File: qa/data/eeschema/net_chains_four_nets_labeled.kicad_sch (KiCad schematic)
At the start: 4 parts

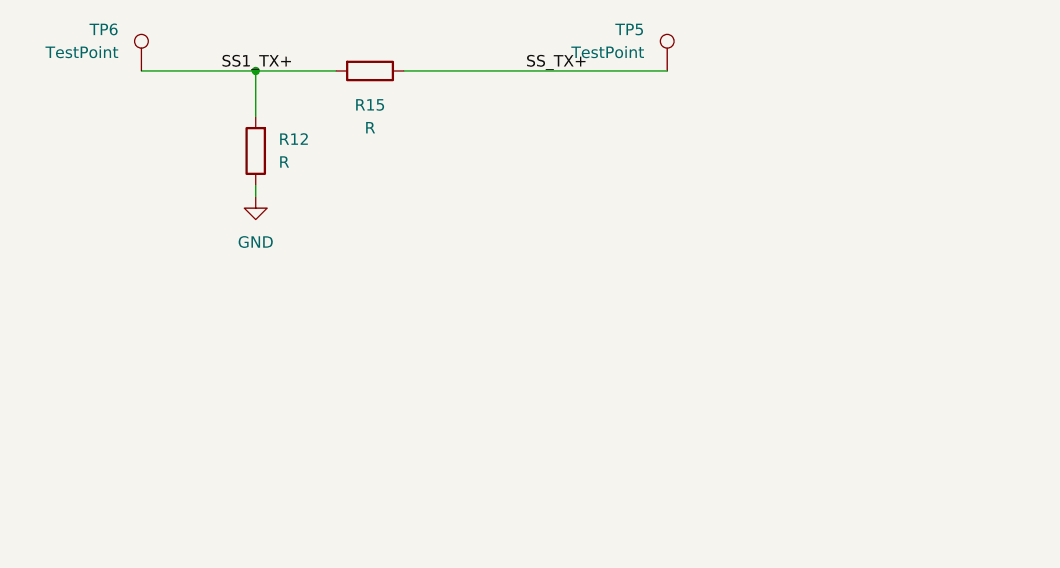
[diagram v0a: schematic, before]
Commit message: Fully rename signals to netchain
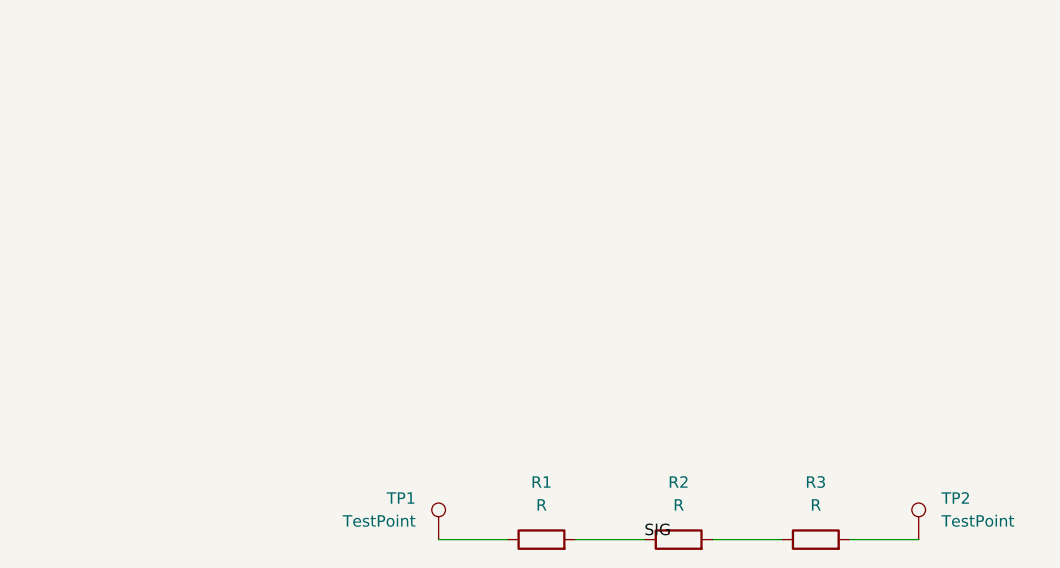
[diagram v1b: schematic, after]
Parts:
- removed R12, R15: R, Resistor_SMD:R_0603_1608Metric, symbol Device:R
- removed TP5, TP6: TestPoint, MountingHole:MountingHole_2.2mm_M2_DIN965_Pad, symbol Connector:TestPoint
- added R1, R2, R3: R, symbol Device:R
- added TP1, TP2: TestPoint, symbol Connector:TestPoint
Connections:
- new net: R1.1, TP1.1
- new net: R2.2, R3.1
- new net: R3.2, TP2.1
- new net SIG: R1.2, R2.1
